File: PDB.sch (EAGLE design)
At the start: 75 parts

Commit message: Last time forget to save. This is the real version of last commit.
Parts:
- removed ADD1_OUT, HAZR_OUT: POWERPOLE_POWER25A_HORIZONTAL_G2, powerpoles:POWERPOLE_POWER25A_HORIZONTAL_G2
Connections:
- removed net N$17: ADD1.D, ADD1_OUT.GND
- net HAZ_R_SIG: no longer HAZR_OUT.GND
- net VDD: no longer ADD1_OUT.V+, HAZR_OUT.V+
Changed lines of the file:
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@@
 <part name="VDD_IN" library="powerpoles" deviceset="POWERPOLE_POWER" device="25A_HORIZONTAL_G2" value="POWERPOLE_POWER25A_HORIZONTAL_G2"/>
 <part name="ADD1" library="master_library" deviceset="NCV8405A" device="DPAK-3PIN" package3d_urn="urn:adsk.eagle:package:8893803/1"/>
-<part name="ADD1_OUT" library="powerpoles" deviceset="POWERPOLE_POWER" device="25A_HORIZONTAL_G2" value="POWERPOLE_POWER25A_HORIZONTAL_G2"/>
 <part name="SUPPLY11" library="supply2" library_urn="urn:adsk.eagle:library:372" deviceset="VDD" device=""/>
 <part name="SUPPLY28" library="supply2" library_urn="urn:adsk.eagle:library:372" deviceset="GND" device=""/>
@@
 <part name="SUPPLY30" library="supply2" library_urn="urn:adsk.eagle:library:372" deviceset="GND" device=""/>
 <part name="HAZ_L" library="master_library" deviceset="NCV8405A" device="DPAK-3PIN" package3d_urn="urn:adsk.eagle:package:8893803/1"/>
-<part name="SUPPLY31" library="supply2" library_urn="urn:adsk.eagle:library:372" deviceset="VDD" device=""/>
 <part name="HAZ_R" library="master_library" deviceset="NCV8405A" device="DPAK-3PIN" package3d_urn="urn:adsk.eagle:package:8893803/1"/>
-<part name="HAZR_OUT" library="powerpoles" deviceset="POWERPOLE_POWER" device="25A_HORIZONTAL_G2" value="POWERPOLE_POWER25A_HORIZONTAL_G2"/>
-<part name="SUPPLY33" library="supply2" library_urn="urn:adsk.eagle:library:372" deviceset="VDD" device=""/>
 <part name="BRAKE" library="master_library" deviceset="NCV8405A" device="DPAK-3PIN" package3d_urn="urn:adsk.eagle:package:8893803/1"/>
 <part name="BRAKE_OUT" library="powerpoles" deviceset="POWERPOLE_POWER" device="25A_HORIZONTAL_G2" value="POWERPOLE_POWER25A_HORIZONTAL_G2"/>
@@
 <attribute name="NAME" x="-48.708375" y="30.48" size="1.778" layer="95" font="vector"/>
 </instance>
-<instance part="ADD1_OUT" gate="G$1" x="-10.16" y="45.72" smashed="yes">
-<attribute name="NAME" x="-15.367" y="53.594" size="1.778" layer="94" rot="SR0"/>
-</instance>
 <instance part="SUPPLY11" gate="G$1" x="-20.32" y="63.5" smashed="yes"/>
 <instance part="SUPPLY28" gate="GND" x="-20.32" y="12.7" smashed="yes"/>
@@
 <attribute name="NAME" x="53.096034375" y="35.814" size="1.778" layer="95" font="vector" rot="SR0"/>
 </instance>
-<instance part="SUPPLY31" gate="G$1" x="63.5" y="63.5" smashed="yes"/>
 <instance part="HAZ_R" gate="G$1" x="86.36" y="27.94" smashed="yes">
 <attribute name="NAME" x="91.196034375" y="35.814" size="1.778" layer="95" font="vector" rot="SR0"/>
 </instance>
-<instance part="HAZR_OUT" gate="G$1" x="111.76" y="45.72" smashed="yes">
-<attribute name="NAME" x="106.553" y="53.594" size="1.778" layer="94" rot="SR0"/>
-</instance>
-<instance part="SUPPLY33" gate="G$1" x="101.6" y="63.5" smashed="yes"/>
 <instance part="BRAKE" gate="G$1" x="119.38" y="27.94" smashed="yes">
 <attribute name="NAME" x="124.216034375" y="35.814" size="1.778" layer="95" font="vector" rot="SR0"/>
@@
 <net name="VDD" class="0">
 <segment>
-<pinref part="SUPPLY31" gate="G$1" pin="VDD"/>
-<wire x1="63.5" y1="50.8" x2="63.5" y2="60.96" width="0.1524" layer="91"/>
-</segment>
-<segment>
-<pinref part="SUPPLY33" gate="G$1" pin="VDD"/>
-<pinref part="HAZR_OUT" gate="G$1" pin="V+"/>
-<wire x1="101.6" y1="50.8" x2="101.6" y2="60.96" width="0.1524" layer="91"/>
-</segment>
-<segment>
 <pinref part="SUPPLY1" gate="G$1" pin="VDD"/>
 <pinref part="HEADLIGHTS_OUT" gate="G$1" pin="V+"/>
@@
 <segment>
 <pinref part="SUPPLY11" gate="G$1" pin="VDD"/>
-<pinref part="ADD1_OUT" gate="G$1" pin="V+"/>
 <wire x1="-20.32" y1="50.8" x2="-20.32" y2="60.96" width="0.1524" layer="91"/>
 </segment>
@@
 </segment>
 </net>
-<net name="N$17" class="0">
-<segment>
-<pinref part="ADD1" gate="G$1" pin="D"/>
-<pinref part="ADD1_OUT" gate="G$1" pin="GND"/>
-</segment>
-</net>
 <net name="N$19" class="0">
 <segment>
@@
 <segment>
 <pinref part="HAZ_R" gate="G$1" pin="D"/>
-<pinref part="HAZR_OUT" gate="G$1" pin="GND"/>
-</segment>
-</net>
+<wire x1="101.6" y1="40.64" x2="101.6" y2="43.18" width="0.1524" layer="91"/>
+<label x="101.6" y="43.18" size="1.778" layer="95"/>
+</segment>
+</net>

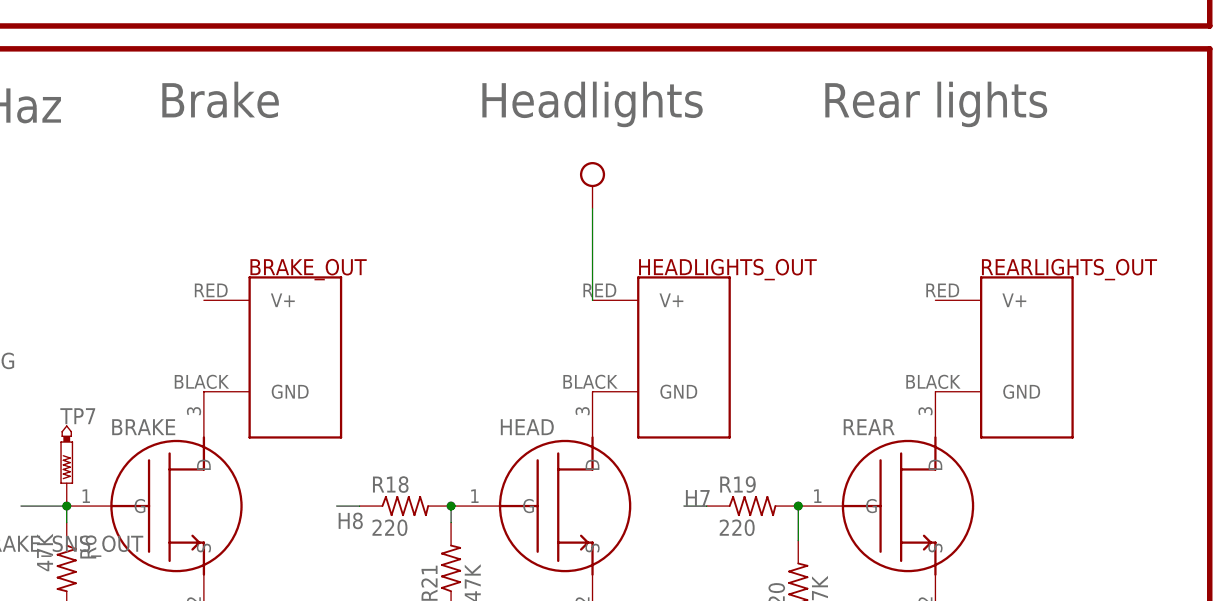
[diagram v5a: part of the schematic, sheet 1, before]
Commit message: Deleted most Anderson connectors. Brake sensor waiting to be modified
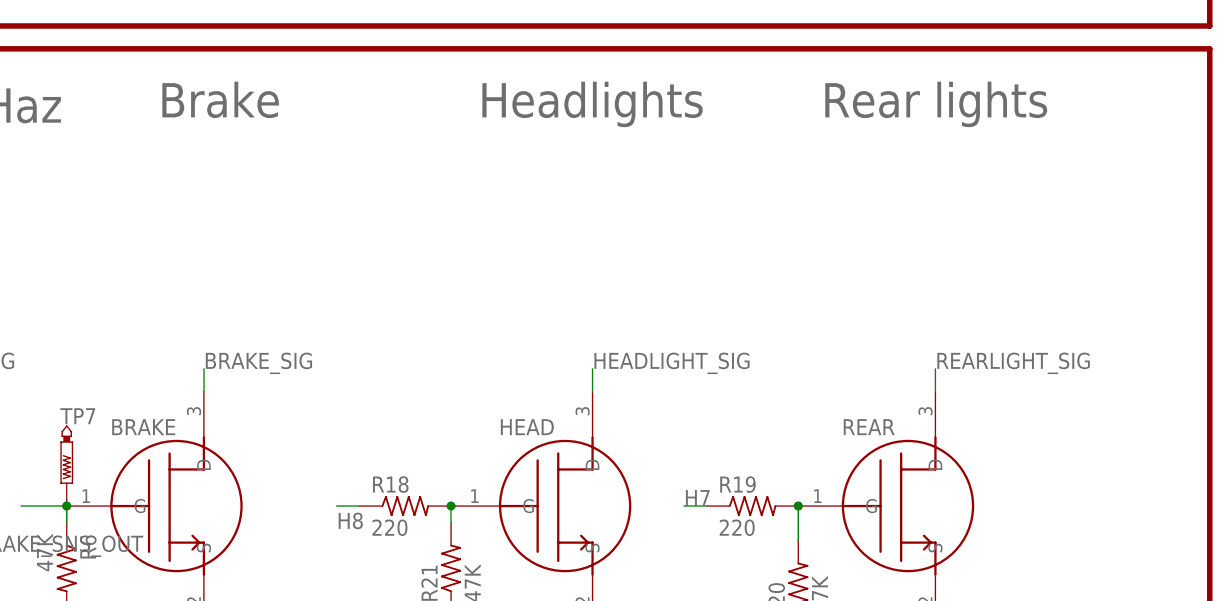
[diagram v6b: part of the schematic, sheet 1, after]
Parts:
- removed BRAKE_OUT, HEADLIGHTS_OUT, REARLIGHTS_OUT: POWERPOLE_POWER25A_HORIZONTAL_G2, powerpoles:POWERPOLE_POWER25A_HORIZONTAL_G2
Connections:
- net BRAKE_SIG: no longer BRAKE_OUT.GND
- net HEADLIGHT_SIG: no longer HEADLIGHTS_OUT.GND
- net REARLIGHT_SIG: no longer REARLIGHTS_OUT.GND
- net VDD: no longer HEADLIGHTS_OUT.V+
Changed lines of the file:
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@@
 <part name="HAZ_R" library="master_library" deviceset="NCV8405A" device="DPAK-3PIN" package3d_urn="urn:adsk.eagle:package:8893803/1"/>
 <part name="BRAKE" library="master_library" deviceset="NCV8405A" device="DPAK-3PIN" package3d_urn="urn:adsk.eagle:package:8893803/1"/>
-<part name="BRAKE_OUT" library="powerpoles" deviceset="POWERPOLE_POWER" device="25A_HORIZONTAL_G2" value="POWERPOLE_POWER25A_HORIZONTAL_G2"/>
 <part name="SUPPLY36" library="supply2" library_urn="urn:adsk.eagle:library:372" deviceset="GND" device=""/>
 <part name="HEAD" library="master_library" deviceset="NCV8405A" device="DPAK-3PIN" package3d_urn="urn:adsk.eagle:package:8893803/1"/>
-<part name="HEADLIGHTS_OUT" library="powerpoles" deviceset="POWERPOLE_POWER" device="25A_HORIZONTAL_G2" value="POWERPOLE_POWER25A_HORIZONTAL_G2"/>
-<part name="SUPPLY1" library="supply2" library_urn="urn:adsk.eagle:library:372" deviceset="VDD" device=""/>
 <part name="SUPPLY2" library="supply2" library_urn="urn:adsk.eagle:library:372" deviceset="GND" device=""/>
 <part name="REAR" library="master_library" deviceset="NCV8405A" device="DPAK-3PIN" package3d_urn="urn:adsk.eagle:package:8893803/1"/>
-<part name="REARLIGHTS_OUT" library="powerpoles" deviceset="POWERPOLE_POWER" device="25A_HORIZONTAL_G2" value="POWERPOLE_POWER25A_HORIZONTAL_G2"/>
 <part name="SUPPLY4" library="supply2" library_urn="urn:adsk.eagle:library:372" deviceset="GND" device=""/>
 <part name="R2" library="rcl" library_urn="urn:adsk.eagle:library:334" deviceset="R-US_" device="R0805" package3d_urn="urn:adsk.eagle:package:23553/2" value="4.7K"/>
@@
 <attribute name="NAME" x="124.216034375" y="35.814" size="1.778" layer="95" font="vector" rot="SR0"/>
 </instance>
-<instance part="BRAKE_OUT" gate="G$1" x="144.78" y="45.72" smashed="yes">
-<attribute name="NAME" x="139.573" y="53.594" size="1.778" layer="94" rot="SR0"/>
-</instance>
 <instance part="SUPPLY36" gate="GND" x="134.62" y="10.16" smashed="yes"/>
 <instance part="HEAD" gate="G$1" x="162.56" y="27.94" smashed="yes">
 <attribute name="NAME" x="167.396034375" y="35.814" size="1.778" layer="95" font="vector" rot="SR0"/>
 </instance>
-<instance part="HEADLIGHTS_OUT" gate="G$1" x="187.96" y="45.72" smashed="yes">
-<attribute name="NAME" x="182.753" y="53.594" size="1.778" layer="94" rot="SR0"/>
-</instance>
-<instance part="SUPPLY1" gate="G$1" x="177.8" y="63.5" smashed="yes"/>
 <instance part="SUPPLY2" gate="GND" x="177.8" y="12.7" smashed="yes"/>
 <instance part="REAR" gate="G$1" x="200.66" y="27.94" smashed="yes">
 <attribute name="NAME" x="205.496034375" y="35.814" size="1.778" layer="95" font="vector" rot="SR0"/>
-</instance>
-<instance part="REARLIGHTS_OUT" gate="G$1" x="226.06" y="45.72" smashed="yes">
-<attribute name="NAME" x="220.853" y="53.594" size="1.778" layer="94" rot="SR0"/>
 </instance>
 <instance part="SUPPLY4" gate="GND" x="215.9" y="12.7" smashed="yes"/>
@@
 <net name="VDD" class="0">
 <segment>
-<pinref part="SUPPLY1" gate="G$1" pin="VDD"/>
-<pinref part="HEADLIGHTS_OUT" gate="G$1" pin="V+"/>
-<wire x1="177.8" y1="50.8" x2="177.8" y2="60.96" width="0.1524" layer="91"/>
-</segment>
-<segment>
 <pinref part="SUPPLY11" gate="G$1" pin="VDD"/>
 <wire x1="-20.32" y1="50.8" x2="-20.32" y2="60.96" width="0.1524" layer="91"/>
@@
 <net name="BRAKE_SIG" class="0">
 <segment>
-<pinref part="BRAKE" gate="G$1" pin="D"/>
-<pinref part="BRAKE_OUT" gate="G$1" pin="GND"/>
-</segment>
-<segment>
 <pinref part="LIGHTS" gate="G$1" pin="P$1"/>
 <wire x1="221.765" y1="127" x2="224.305" y2="127" width="0.1524" layer="91"/>
 <label x="224.305" y="127" size="1.778" layer="95"/>
 </segment>
+<segment>
+<pinref part="BRAKE" gate="G$1" pin="D"/>
+<wire x1="134.62" y1="40.64" x2="134.62" y2="43.18" width="0.1524" layer="91"/>
+<label x="134.62" y="43.18" size="1.778" layer="95"/>
+</segment>
 </net>
 <net name="HEADLIGHT_SIG" class="0">
-<segment>
-<pinref part="HEAD" gate="G$1" pin="D"/>
-<pinref part="HEADLIGHTS_OUT" gate="G$1" pin="GND"/>
-</segment>
 <segment>
 <pinref part="LIGHTS" gate="G$1" pin="P$4"/>
@@
 <label x="224.305" y="111.76" size="1.778" layer="95"/>
 </segment>
+<segment>
+<pinref part="HEAD" gate="G$1" pin="D"/>
+<wire x1="177.8" y1="40.64" x2="177.8" y2="43.18" width="0.1524" layer="91"/>
+<label x="177.8" y="43.18" size="1.778" layer="95"/>
+</segment>
 </net>
 <net name="REARLIGHT_SIG" class="0">
-<segment>
-<pinref part="REAR" gate="G$1" pin="D"/>
-<pinref part="REARLIGHTS_OUT" gate="G$1" pin="GND"/>
-</segment>
 <segment>
 <pinref part="LIGHTS" gate="G$1" pin="P$5"/>
@@
 <label x="224.305" y="106.68" size="1.778" layer="95"/>
 </segment>
+<segment>
+<pinref part="REAR" gate="G$1" pin="D"/>
+<wire x1="215.9" y1="40.64" x2="215.9" y2="43.18" width="0.1524" layer="91"/>
+<label x="215.9" y="43.18" size="1.778" layer="95"/>
+</segment>
 </net>

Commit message: adds new connectors and relays, and removes old connectors and wiper fet
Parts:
- removed 555: LM555N, linear:LM555N
- removed C1: 33uF, rcl:C-USC0805
- removed C10, C4: 22uF, SparkFun-Capacitors:22UF-POLAR-PANASONIC_C-35V-20%
- removed C2: 0.01uF, rcl:C-USC0805
- removed C3: 10uF, rcl:C-USC0805
- removed D1: 15V, diode:ZENER-DIODEDO41Z10
- removed D2: 1N4446, diode:1N4446
- removed R10: 1K, rcl:R-US_R0805
- removed R11: 10K, pot:TRIM_US-B25U
- removed R14: 220, rcl:R-US_R0805
- removed R15: 5K, rcl:R-US_R0805
- removed R3: 4.7K, rcl:R-US_R0805
- removed TP1, TP4: PTR1B2,54, testpad:PTR1B2,54
- removed VDD_IN, VDD_IN1, WIPER_OUT: POWERPOLE_POWER25A_HORIZONTAL_G2, powerpoles:POWERPOLE_POWER25A_HORIZONTAL_G2
- removed WIPER_: NCV8405ADPAK-3PIN, master_library:NCV8405ADPAK-3PIN
- added HORN: (no value), switch:M9040P
- added J1, J2, J5: B06B-HCMKK, AUX Lib:B06B-HCMKK
- added J3, J4: SS-6488-NF-A431, AUX Lib:SS-6488-NF-A431
- added J6, J7: B03B-HCMKS, AUX Lib:B03B-HCMKS
- added POWER1: (no value), led:LEDCHIPLED_0805
- added R1: 470, resistor:R-US_R3225
- added U$3: (no value), AUX Lib:TEENSY-3.6_ONLY_HOLES
- added U$4: KEYSTONE_FUSE_3522, AUX Lib:KEYSTONE_FUSE_3522
- added U$5, U$6: TE_CON_OJE-SH-112DM,095\, AUX Lib:TE_CON_OJE-SH-112DM,095\
- U$2: value BLADEFUSE -> KEYSTONE_FUSE_3522; device master_library:BLADEFUSE -> AUX Lib:KEYSTONE_FUSE_3522
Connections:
- removed net 12V_IN: U$2.2, U$2.P$2, VDD_IN.V+
- removed net BRAKE_SNS_OUT: BRAKE.G, R6.1, TP7.TP, U$1.1, VDD_IN1.GND
- removed net CV: 555.CV, C2.1
- removed net DIS: 555.DIS, R10.1, R15.1
- removed net N$19: D2.A, WIPER_.D, WIPER_OUT.GND
- removed net N$22: R14.2, R3.1, TP4.TP, WIPER_.G
- removed net N$6: R11.A, R15.2
- removed net TR/THR: 555.THR, C3.1, R11.S
- new net 3.3V: J3.1, J4.1
- new net 5V: J7.1
- new net BRAKE_SNS: BRAKE.G, J6.2, R6.1, TP7.TP, U$1.1
- new net CLK_A: J3.4
- new net CLK_B: J4.4
- new net H9: HORN.O, U$5.CLA
- new net HORN: U$5.SWB
- new net IGND: J2.6, J5.5, R1.2
- new net ISOENABLE: J5.3
- new net IVDD: J2.1, POWER1.A, U$4.2, U$5.SWA, U$6.SWA
- new net MISO_A: J3.5
- new net MISO_B: J4.5
- new net MOSI_A: J3.3
- new net MOSI_B: J4.3
- new net N$10: POWER1.C, R1.1
- new net N$7: J5.1, U$2.2
- new net N$8: J5.2, U$4.1
- new net PEDAL_SNS: J7.2
- new net WIPER: U$6.SWB
- net 10V_REG: now also HORN.P; no longer 555.R, 555.V+, C4.+, R10.2
- net 555_OUT: no longer TP1.TP
- net 5V_REG: now also J6.1, U$3.VIN(3.6-6V); no longer VDD_IN1.V+
- net GND: now also J1.6, J3.2, J4.2, J5.6, J7.3, U$3.GND@1, U$3.GND@2, U$5.CLB, U$6.CLB; no longer 555.GND, C1.2, C10.-, C2.2, C3.2, C4.-, D1.A, R3.2, VDD_IN.GND, WIPER_.S
- net H4: now also U$6.CLA; no longer R14.1
- net VDD: now also ADD1.D, J1.1; no longer C10.+, D1.C, D2.C, U$2.P$1, WIPER_OUT.V+
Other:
- note removed: "555 Timer"
- moved on the sheet: ADD1, R13, R2, R9, TP3
